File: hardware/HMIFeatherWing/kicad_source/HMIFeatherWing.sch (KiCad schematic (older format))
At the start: 25 parts, among them CN1 ARDUINO_MKR, Q1 2N7002, SW1 ALPS_SKRH, SW6 TAST_VER

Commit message: made schematic and layout
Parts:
- removed CN1: ARDUINO_MKR, MODULE_compute:ARDUINO_MKR_HOLES, symbol MODULE_compute:ARDUINO_MKR
- added CN1: ADAFRUIT_FEATHER, MODULE_compute:ADAFRUIT_FEATHER_HOLES, symbol MODULE_compute:ADAFRUIT_FEATHER
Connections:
- wire segments 114 -> 116
- no-connect marks 15 -> 17
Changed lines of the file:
@@
-$EndComp
-$Comp
-L MODULE_compute:ARDUINO_MKR CN1
-U 1 1 5DBCD741
-P 9000 3250
-F 0 "CN1" H 9000 4147 60  0000 C CNN
-F 1 "ARDUINO_MKR" H 9000 4041 60  0000 C CNN
-F 2 "MODULE_compute:ARDUINO_MKR_HOLES" H 8900 3900 60  0001 C CNN
-F 3 "" H 9000 2950 60  0000 C CNN
-	1    9000 3250
-	1    0    0    -1
 $EndComp
 $Comp
@@
 	1    0    0    -1
 $EndComp
-Wire Wire Line
-	10250 3700 9600 3700
-Wire Wire Line
-	10250 3600 9600 3600
-Text Label 9750 3700 0    60   ~ 0
+Text Label 7850 3450 0    60   ~ 0
 DIS_SI
-Text Label 9750 3600 0    60   ~ 0
+Text Label 7850 3350 0    60   ~ 0
 DIS_CLK
-Wire Wire Line
-	10250 3000 9600 3000
-Wire Wire Line
-	7550 2700 8400 2700
-Text Label 7650 2700 0    60   ~ 0
+Text Label 7850 2750 0    60   ~ 0
 KEYPAD_A0
-Text Label 9750 3000 0    60   ~ 0
+Text Label 8100 2350 0    60   ~ 0
 RESET
-NoConn ~ 9600 2600
-NoConn ~ 9600 2700
 $Comp
 L HMIFeatherWing-rescue:GND-ArduHMIShield-rescue-ArduHMIShield-rescue-MKRHMIShield-rescue-MKRHMIShield-rescue #PWR0105
 U 1 1 5DC0F0A4
-P 9650 3950
-F 0 "#PWR0105" H 9650 3700 50  0001 C CNN
-F 1 "GND" H 9650 3800 50  0000 C CNN
-F 2 "" H 9650 3950 50  0000 C CNN
-F 3 "" H 9650 3950 50  0000 C CNN
-	1    9650 3950
+P 8450 3950
+F 0 "#PWR0105" H 8450 3700 50  0001 C CNN
+F 1 "GND" H 8450 3800 50  0000 C CNN
+F 2 "" H 8450 3950 50  0000 C CNN
+F 3 "" H 8450 3950 50  0000 C CNN
+	1    8450 3950
 	1    0    0    -1
 $EndComp
@@
 L HMIFeatherWing-rescue:+3V3-power-supply-MKRHMIShield-rescue-MKRHMIShield-rescue #PWR0106
 U 1 1 5DC10F3C
-P 9700 2500
-F 0 "#PWR0106" H 9700 2350 50  0001 C CNN
-F 1 "+3V3" V 9715 2628 50  0000 L CNN
-F 2 "" H 9700 2500 50  0000 C CNN
-F 3 "" H 9700 2500 50  0000 C CNN
-	1    9700 2500
+P 8450 2200
+F 0 "#PWR0106" H 8450 2050 50  0001 C CNN
+F 1 "+3V3" V 8465 2328 50  0000 L CNN
+F 2 "" H 8450 2200 50  0000 C CNN
+F 3 "" H 8450 2200 50  0000 C CNN
+	1    8450 2200
 	1    0    0    -1
 $EndComp
-Wire Wire Line
-	9600 2800 9700 2800
-Wire Wire Line
-	9700 2800 9700 2500
-Wire Wire Line
-	9600 2900 9650 2900
-Wire Wire Line
-	9650 2900 9650 3950
-NoConn ~ 9600 3100
-NoConn ~ 9600 3200
-NoConn ~ 9600 3300
-NoConn ~ 9600 3400
-NoConn ~ 9600 3500
-NoConn ~ 8400 2600
-NoConn ~ 8400 3000
-NoConn ~ 8400 3100
-NoConn ~ 8400 3600
-NoConn ~ 8400 3700
-NoConn ~ 8400 3800
-NoConn ~ 8400 3900
-NoConn ~ 9600 3900
-Wire Wire Line
-	10250 3800 9600 3800
-Text Label 9750 3800 0    60   ~ 0
+Text Label 9850 3050 0    60   ~ 0
 DIS_CS
-Wire Wire Line
-	7550 3400 8400 3400
-Wire Wire Line
-	7550 3500 8400 3500
-Text Label 7600 3400 0    60   ~ 0
+Text Label 9850 3250 0    60   ~ 0
 DIS_A0
-Text Label 7600 3500 0    60   ~ 0
+Text Label 9850 3350 0    60   ~ 0
 DIS_RESET
-Wire Wire Line
-	7550 3300 8400 3300
-Text Label 7600 3300 0    60   ~ 0
+Text Label 9850 3150 0    60   ~ 0
 DISPLAY_BL
 $Comp
@@
 Text Notes 1150 7600 0    47   ~ 0
 multicomp MCMT5 should also be OK\nhttps://de.farnell.com/multicomp/mcmt5-f-v/navigationsschalter-5polig-smd/dp/1316987
+$Comp
+L MODULE_compute:ADAFRUIT_FEATHER CN1
+U 1 1 5DD44785
+P 9150 3100
+F 0 "CN1" H 9150 4097 60  0000 C CNN
+F 1 "ADAFRUIT_FEATHER" H 9150 3991 60  0000 C CNN
+F 2 "MODULE_compute:ADAFRUIT_FEATHER_HOLES" H 9300 3850 60  0001 C CNN
+F 3 "" H 9150 2900 60  0000 C CNN
+	1    9150 3100
+	1    0    0    -1
+$EndComp
+Wire Wire Line
+	8550 2650 8450 2650
+Wire Wire Line
+	8450 2650 8450 3850
+Wire Wire Line
+	8550 3850 8450 3850
+Connection ~ 8450 3850
+Wire Wire Line
+	8450 3850 8450 3950
+Wire Wire Line
+	8050 2350 8550 2350
+Wire Wire Line
+	8550 2450 8450 2450
+Wire Wire Line
+	8450 2450 8450 2200
+Wire Wire Line
+	7800 2750 8550 2750
+Wire Wire Line
+	7800 3350 8550 3350
+Wire Wire Line
+	7800 3450 8550 3450
+Wire Wire Line
+	10400 3050 9750 3050
+Wire Wire Line
+	10400 3150 9750 3150
+Wire Wire Line
+	10400 3250 9750 3250
+Wire Wire Line
+	10400 3350 9750 3350
+NoConn ~ 8550 2550
+NoConn ~ 8550 2850
+NoConn ~ 8550 2950
+NoConn ~ 8550 3050
+NoConn ~ 8550 3150
+NoConn ~ 8550 3250
+NoConn ~ 8550 3550
+NoConn ~ 8550 3650
+NoConn ~ 8550 3750
+NoConn ~ 9750 3850
+NoConn ~ 9750 3750
+NoConn ~ 9750 3650
+NoConn ~ 9750 3550
+NoConn ~ 9750 3450
+NoConn ~ 9750 2950
+NoConn ~ 9750 2850
+NoConn ~ 9750 2750
 $EndSCHEMATC

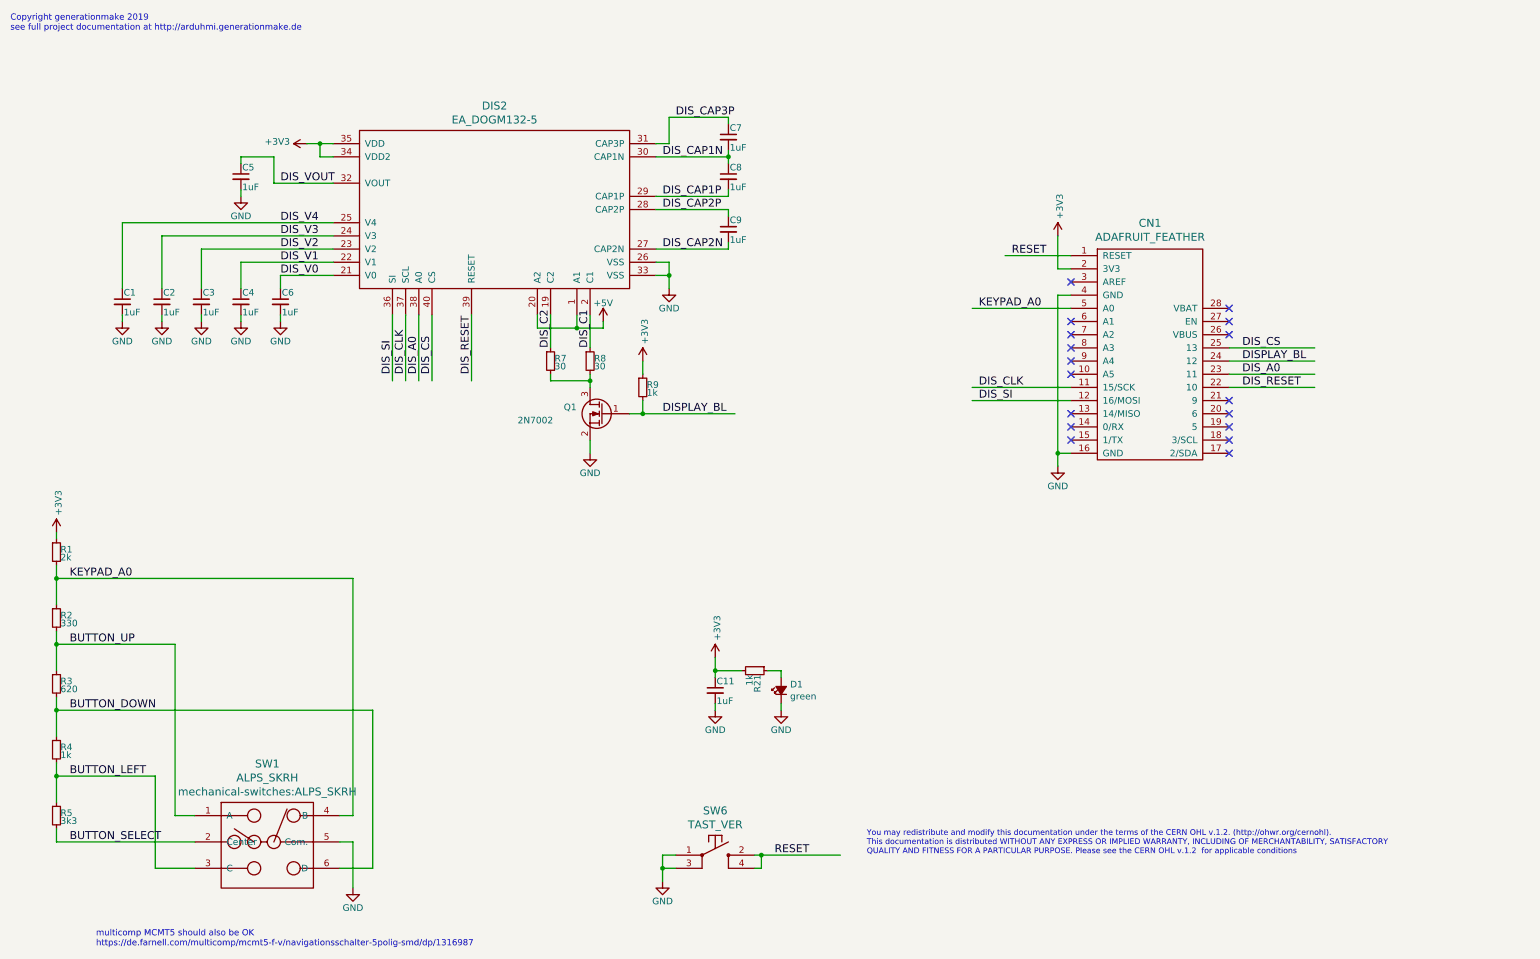
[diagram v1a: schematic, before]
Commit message: checked pins to fit to other feather wings, used smaller reset, corrected joystick orientation, connected backlight, made board smaller, finished layout
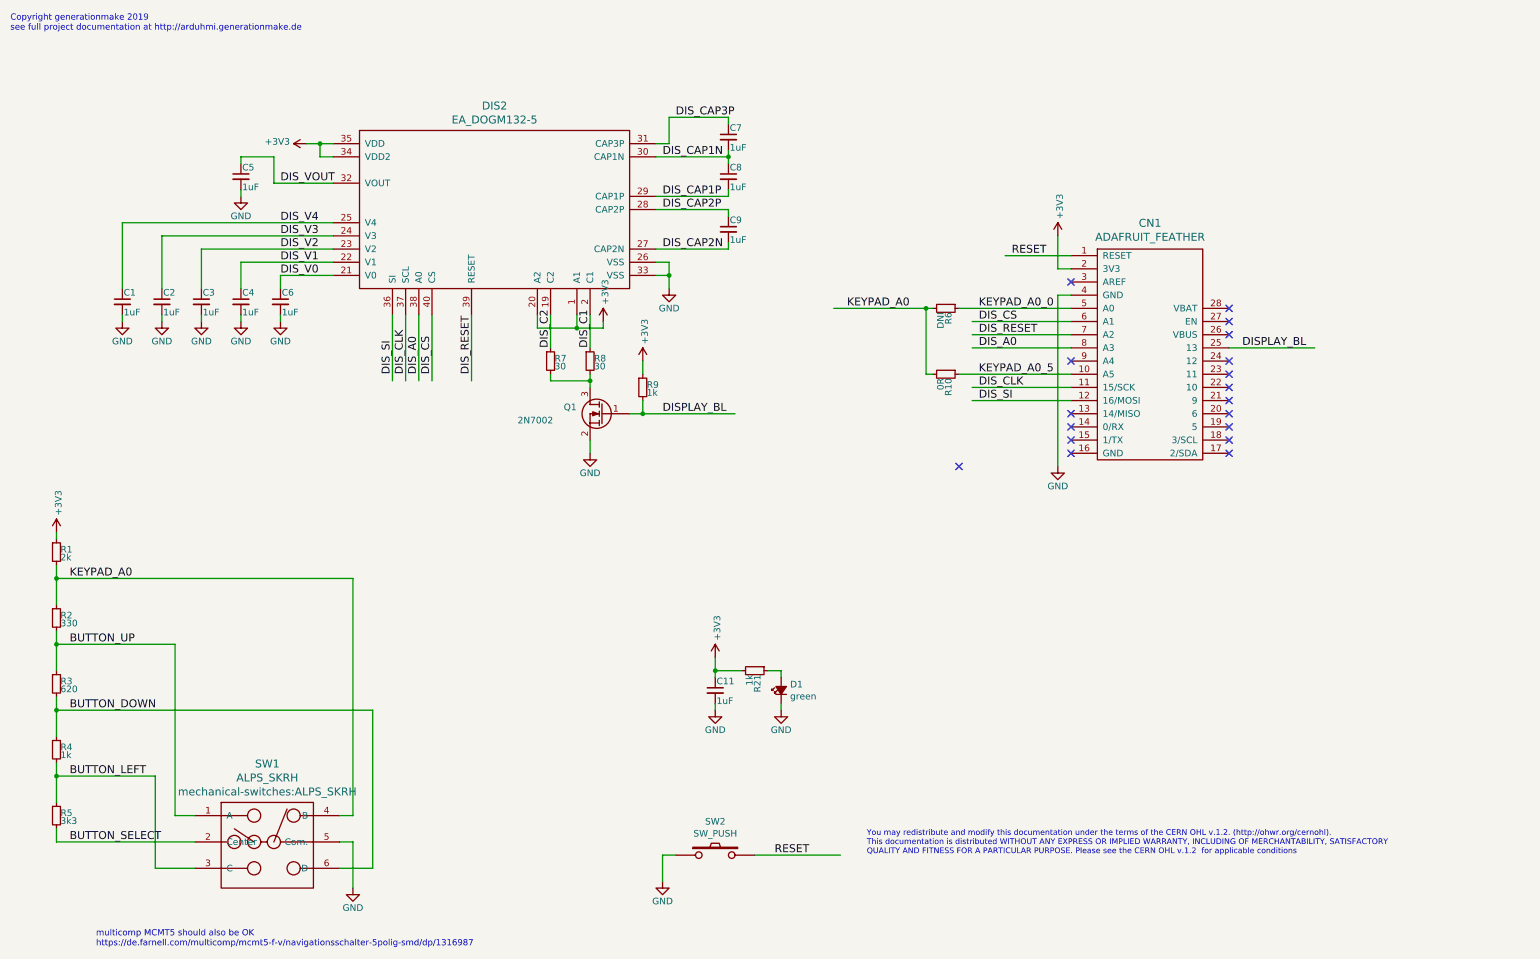
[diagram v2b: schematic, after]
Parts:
- removed SW6: TAST_VER, mechanical-switches:WE_430182050816, symbol HMIFeatherWing-rescue:TAST_VER-mechanical-switches-MKRHMIShield-rescue-MKRHMISh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
- added R10: 0R, resistors:R_0603, symbol HMIFeatherWing-rescue:R_1206-ArduHMIShield-rescue-ArduHMIShield-rescue-MKRHMISh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
- added R6: DNI, resistors:R_0603, symbol HMIFeatherWing-rescue:R_1206-ArduHMIShield-rescue-ArduHMIShield-rescue-MKRHMISh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
- added SW2: SW_PUSH, mechanical-switches:smd_push, symbol devices:SW_PUSH
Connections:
- net labels added: KEYPAD_A0_0, KEYPAD_A0_5
- net labels removed: +5V
- wire segments 116 -> 114
- no-connect marks 17 -> 18
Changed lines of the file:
@@
 EESchema Schematic File Version 4
-LIBS:HMIFeatherWing-cache
 EELAYER 30 0
 EELAYER END
@@
 $EndComp
 $Comp
-L HMIFeatherWing-rescue:+5V-ArduHMIShield-rescue-ArduHMIShield-rescue-MKRHMIShield-rescue-MKRHMIShield-rescue #PWR016
-U 1 1 5B63CEC4
-P 5000 2850
-F 0 "#PWR016" H 5000 2700 50  0001 C CNN
-F 1 "+5V" H 5000 2990 50  0000 C CNN
-F 2 "" H 5000 2850 50  0000 C CNN
-F 3 "" H 5000 2850 50  0000 C CNN
-	1    5000 2850
-	1    0    0    -1
-$EndComp
-$Comp
 L HMIFeatherWing-rescue:GND-ArduHMIShield-rescue-ArduHMIShield-rescue-MKRHMIShield-rescue-MKRHMIShield-rescue #PWR015
 U 1 1 5B63D119
@@
 $EndComp
 Wire Wire Line
-	6800 6900 6200 6900
-Wire Wire Line
-	6150 7000 6200 7000
-Wire Wire Line
-	6200 7000 6200 6900
-Connection ~ 6200 6900
-Wire Wire Line
 	5550 6900 5450 6900
-Wire Wire Line
-	5450 6900 5450 7000
-Wire Wire Line
-	5550 7000 5450 7000
-Connection ~ 5450 7000
 Text Label 6300 6900 0    60   ~ 0
 RESET
 Wire Wire Line
 	5300 3550 5200 3550
-Wire Wire Line
-	6200 6900 6150 6900
-Wire Wire Line
-	5450 7000 5450 7100
 $Comp
 L HMIFeatherWing-rescue:+3V3-power-supply-MKRHMIShield-rescue-MKRHMIShield-rescue #PWR013
@@
 You may redistribute and modify this documentation under the terms of the CERN OHL v.1.2. (http://ohwr.org/cernohl). \nThis documentation is distributed WITHOUT ANY EXPRESS OR IMPLIED WARRANTY, INCLUDING OF MERCHANTABILITY, SATISFACTORY \nQUALITY AND FITNESS FOR A PARTICULAR PURPOSE. Please see the CERN OHL v.1.2  for applicable conditions
 $Comp
-L HMIFeatherWing-rescue:TAST_VER-mechanical-switches-MKRHMIShield-rescue-MKRHMIShield-rescue SW6
-U 1 1 5D125154
-P 5850 6900
-F 0 "SW6" H 5850 7237 60  0000 C CNN
-F 1 "TAST_VER" H 5850 7131 60  0000 C CNN
-F 2 "mechanical-switches:WE_430182050816" H 6700 6950 60  0001 C CNN
-F 3 "" H 6700 6950 60  0000 C CNN
-	1    5850 6900
-	1    0    0    -1
-$EndComp
-$Comp
 L HMIFeatherWing-rescue:+3V3-power-supply-MKRHMIShield-rescue-MKRHMIShield-rescue #PWR0102
 U 1 1 5DBD379E
@@
 Text Label 7850 3350 0    60   ~ 0
 DIS_CLK
-Text Label 7850 2750 0    60   ~ 0
+Text Label 6850 2750 0    60   ~ 0
 KEYPAD_A0
 Text Label 8100 2350 0    60   ~ 0
@@
 	1    0    0    -1
 $EndComp
+Text Label 7850 2850 0    60   ~ 0
+DIS_CS
+Text Label 7850 3050 0    60   ~ 0
+DIS_A0
+Text Label 7850 2950 0    60   ~ 0
+DIS_RESET
 Text Label 9850 3050 0    60   ~ 0
-DIS_CS
-Text Label 9850 3250 0    60   ~ 0
-DIS_A0
-Text Label 9850 3350 0    60   ~ 0
-DIS_RESET
-Text Label 9850 3150 0    60   ~ 0
 DISPLAY_BL
 $Comp
@@
 	8550 2650 8450 2650
 Wire Wire Line
-	8450 2650 8450 3850
-Wire Wire Line
-	8550 3850 8450 3850
-Connection ~ 8450 3850
-Wire Wire Line
-	8450 3850 8450 3950
-Wire Wire Line
 	8050 2350 8550 2350
 Wire Wire Line
@@
 	8450 2450 8450 2200
 Wire Wire Line
-	7800 2750 8550 2750
-Wire Wire Line
 	7800 3350 8550 3350
 Wire Wire Line
@@
 Wire Wire Line
 	10400 3050 9750 3050
-Wire Wire Line
-	10400 3150 9750 3150
-Wire Wire Line
-	10400 3250 9750 3250
-Wire Wire Line
-	10400 3350 9750 3350
 NoConn ~ 8550 2550
-NoConn ~ 8550 2850
-NoConn ~ 8550 2950
-NoConn ~ 8550 3050
 NoConn ~ 8550 3150
-NoConn ~ 8550 3250
 NoConn ~ 8550 3550
 NoConn ~ 8550 3650
@@
 NoConn ~ 9750 2850
 NoConn ~ 9750 2750
+Wire Wire Line
+	8450 2650 8450 3950
+NoConn ~ 8550 3850
+NoConn ~ 7700 3950
+$Comp
+L HMIFeatherWing-rescue:R_1206-ArduHMIShield-rescue-ArduHMIShield-rescue-MKRHMIShield-rescue-MKRHMIShield-rescue R6
+U 1 1 5DE81459
+P 7600 2750
+F 0 "R6" H 7630 2770 50  0000 L CNN
+F 1 "DNI" H 7630 2710 50  0000 L CNN
+F 2 "resistors:R_0603" H 7600 2600 50  0001 C CNN
+F 3 "" H 7600 2750 50  0000 C CNN
+	1    7600 2750
+	0    1    1    0
+$EndComp
+$Comp
+L HMIFeatherWing-rescue:R_1206-ArduHMIShield-rescue-ArduHMIShield-rescue-MKRHMIShield-rescue-MKRHMIShield-rescue R10
+U 1 1 5DE835D8
+P 7600 3250
+F 0 "R10" H 7630 3270 50  0000 L CNN
+F 1 "0R" H 7630 3210 50  0000 L CNN
+F 2 "resistors:R_0603" H 7600 3100 50  0001 C CNN
+F 3 "" H 7600 3250 50  0000 C CNN
+	1    7600 3250
+	0    1    1    0
+$EndComp
+Wire Wire Line
+	6750 2750 7450 2750
+Wire Wire Line
+	7450 2750 7450 3250
+Wire Wire Line
+	7450 3250 7500 3250
+Connection ~ 7450 2750
+Wire Wire Line
+	7450 2750 7500 2750
+Wire Wire Line
+	7700 3250 8550 3250
+Wire Wire Line
+	7700 2750 8550 2750
+Text Label 7850 3250 0    60   ~ 0
+KEYPAD_A0_5
+Text Label 7850 2750 0    60   ~ 0
+KEYPAD_A0_0
+Wire Wire Line
+	7800 3050 8550 3050
+Wire Wire Line
+	7800 2950 8550 2950
+Wire Wire Line
+	7800 2850 8550 2850
+NoConn ~ 9750 3350
+NoConn ~ 9750 3250
+NoConn ~ 9750 3150
+$Comp
+L devices:SW_PUSH SW2
+U 1 1 5DEB8D9E
+P 5850 6900
+F 0 "SW2" H 5850 7155 50  0000 C CNN
+F 1 "SW_PUSH" H 5850 7064 50  0000 C CNN
+F 2 "mechanical-switches:smd_push" H 5850 7063 50  0001 C CNN
+F 3 "" H 5850 6900 50  0000 C CNN
+	1    5850 6900
+	1    0    0    -1
+$EndComp
+Wire Wire Line
+	6150 6900 6800 6900
+Wire Wire Line
+	5450 6900 5450 7100
+$Comp
+L HMIFeatherWing-rescue:+3V3-power-supply-MKRHMIShield-rescue-MKRHMIShield-rescue #PWR0108
+U 1 1 5DEC54D8
+P 5000 2850
+F 0 "#PWR0108" H 5000 2700 50  0001 C CNN
+F 1 "+3V3" V 5015 2978 50  0000 L CNN
+F 2 "" H 5000 2850 50  0000 C CNN
+F 3 "" H 5000 2850 50  0000 C CNN
+	1    5000 2850
+	1    0    0    -1
+$EndComp
 $EndSCHEMATC
